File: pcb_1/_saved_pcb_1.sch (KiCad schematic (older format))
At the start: 43 parts, among them J1 Vin, J2 Vout, J3 2N3055_conn, P1 CONN_01X07, P2 CONN_01X01, P3 CONN_01X01, P4 CONN_01X01, P5 CONN_01X01, P6 CONN_01X01, P7 CONN_01X01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

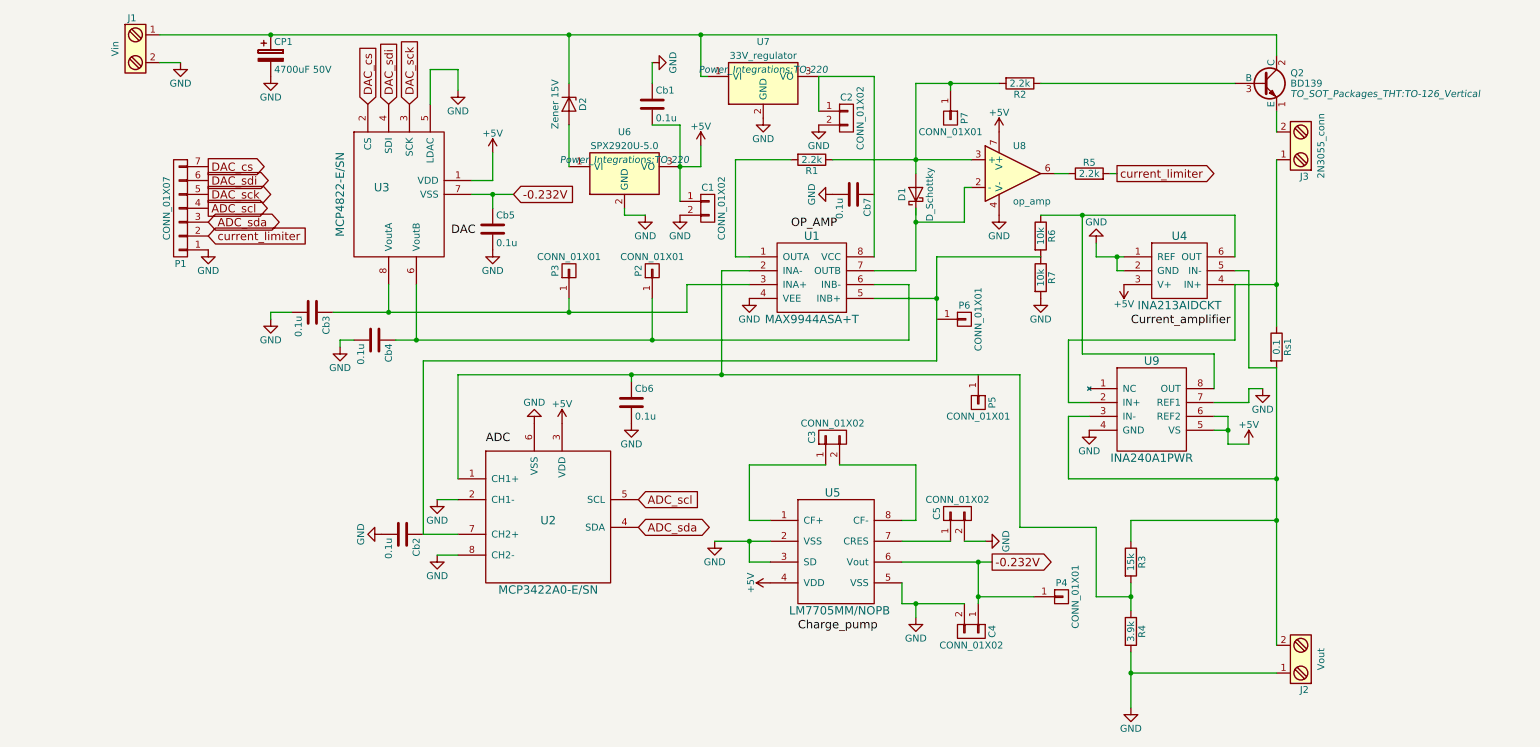
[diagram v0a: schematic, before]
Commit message: AC-input lisätty Footprintit mikropiireille
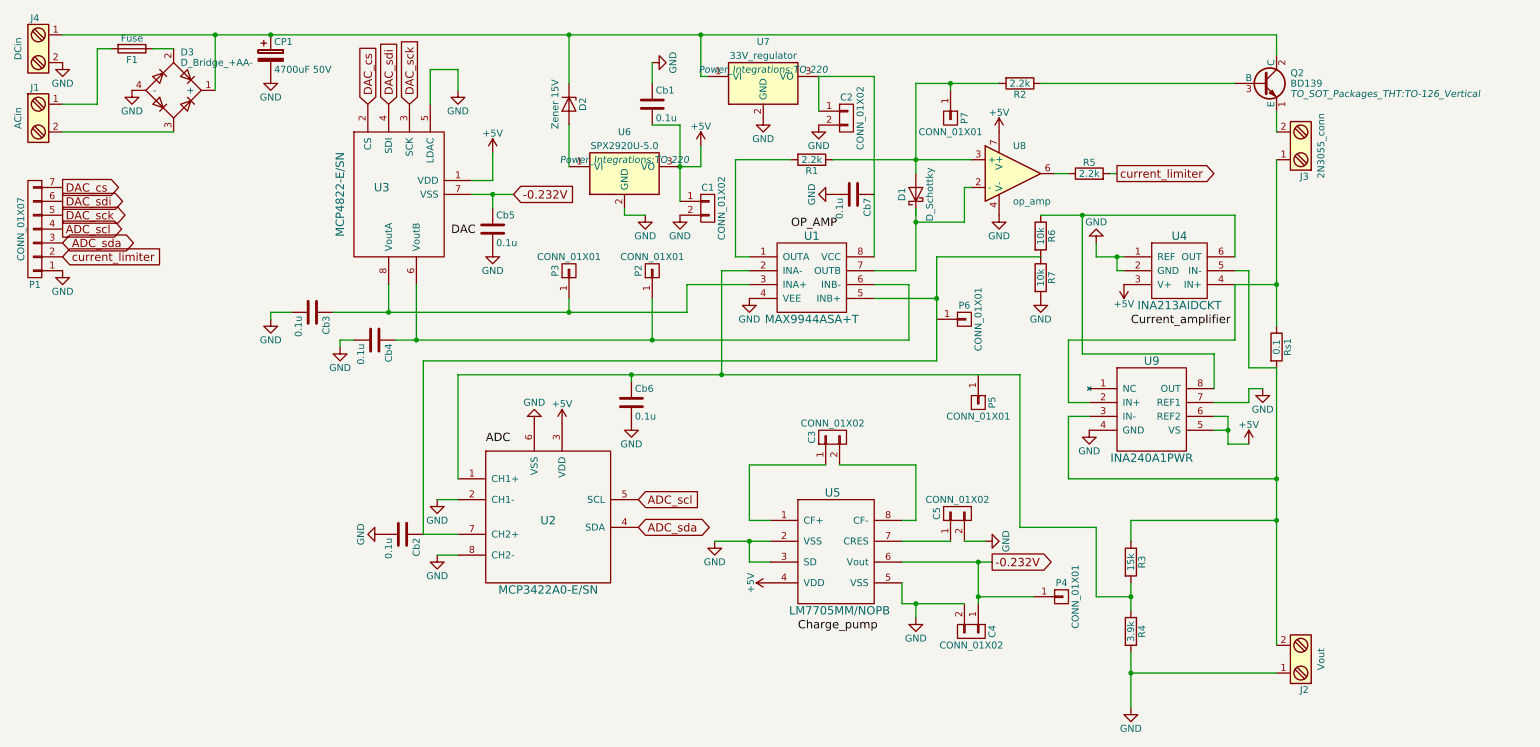
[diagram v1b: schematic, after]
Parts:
- added D3: D_Bridge_+AA-, symbol D_Bridge_+AA-
- added F1: Fuse, symbol Fuse
- added J4: DCin, symbol Screw_Terminal_1x02
- Cb6, Cb7: footprint (none) -> Capacitors_SMD:C_0805_HandSoldering
- J1: value Vin -> ACin
- P2, P3, P4, P5, P6, P7: footprint (none) -> Pin_Headers:Pin_Header_Straight_1x01_Pitch2.54mm
- R6, R7: footprint (none) -> Resistors_SMD:R_0603_HandSoldering
- U1, U2, U3, U5: footprint (none) -> Housings_SSOP:MSOP-8_3x3mm_Pitch0.65mm
- U4: footprint (none) -> TO_SOT_Packages_SMD:SOT-363_SC-70-6_Handsoldering
- U9: footprint (none) -> Housings_SSOP:TSSOP-8_4.4x3mm_Pitch0.65mm
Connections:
- net GND: now also D3.4 (-), J4.2; no longer J1.2
- net at CP1.1, D2.1 (K), Q2.2 (C)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: now also D3.1 (+), J4.1; no longer J1.1
- new net: F1.2, J1.1
- new net: D3.3, J1.2
- new net: D3.2, F1.1
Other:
- moved on the sheet: J1, P1
